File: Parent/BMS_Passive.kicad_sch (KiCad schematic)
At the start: 12 parts, among them U15 TSV911IDT, U16 TSV911IDT, U17 TSV911IDT, U18 TSV911IDT, U31 TSV911IDT, U32 TSV911IDT, U33 TSV911IDT, U34 TSV911IDT

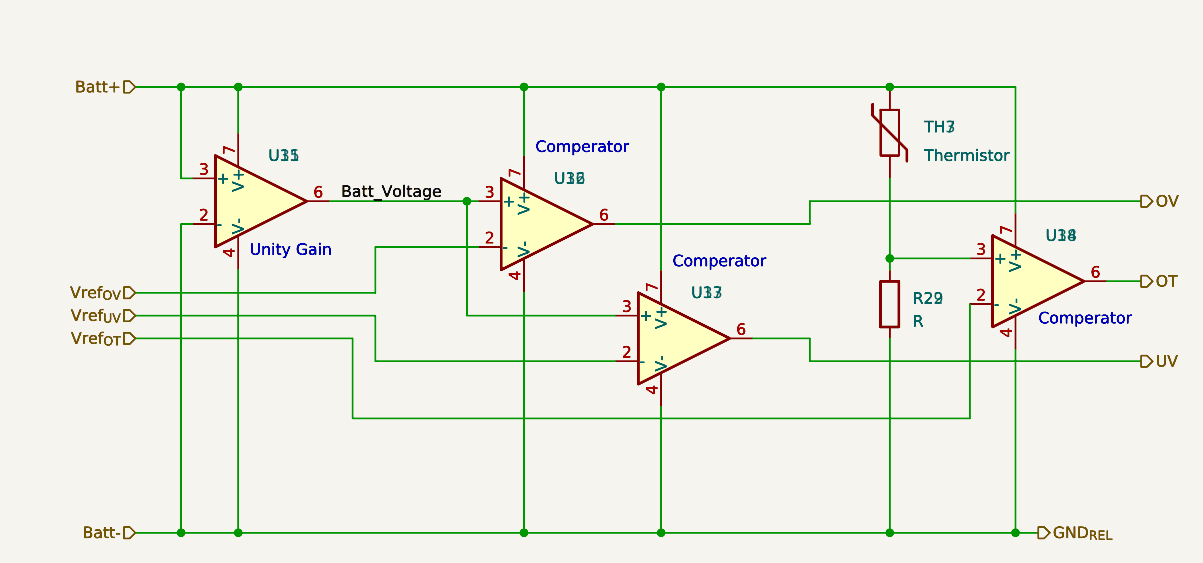
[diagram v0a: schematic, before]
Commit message: Updated Parent further - Move workspace to cloud
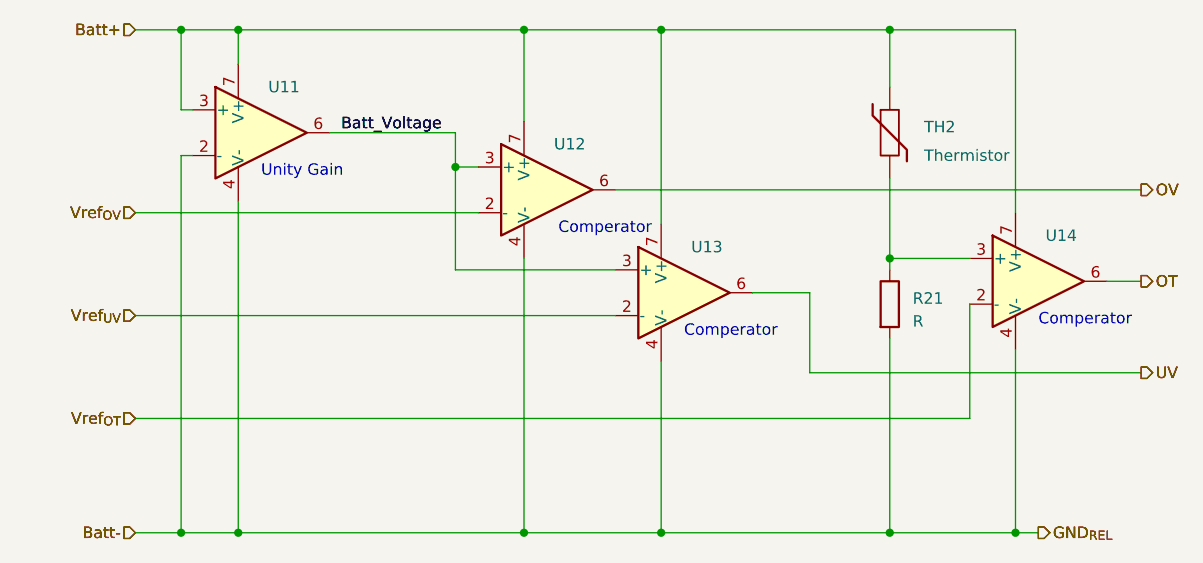
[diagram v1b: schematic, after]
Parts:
- removed R29: R, symbol Device:R
- removed TH7: Thermistor, symbol Device:Thermistor
- removed U15, U16, U33, U34: TSV911IDT, Package_SO:SOIC-8_3.9x4.9mm_P1.27mm, symbol Amplifier_Operational:TSV911IDT
- renumbered R22 to R21, TH3 to TH2, U31 to U11, U32 to U12, U17 to U13, U18 to U14
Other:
- moved on the sheet: U11, U12, U13

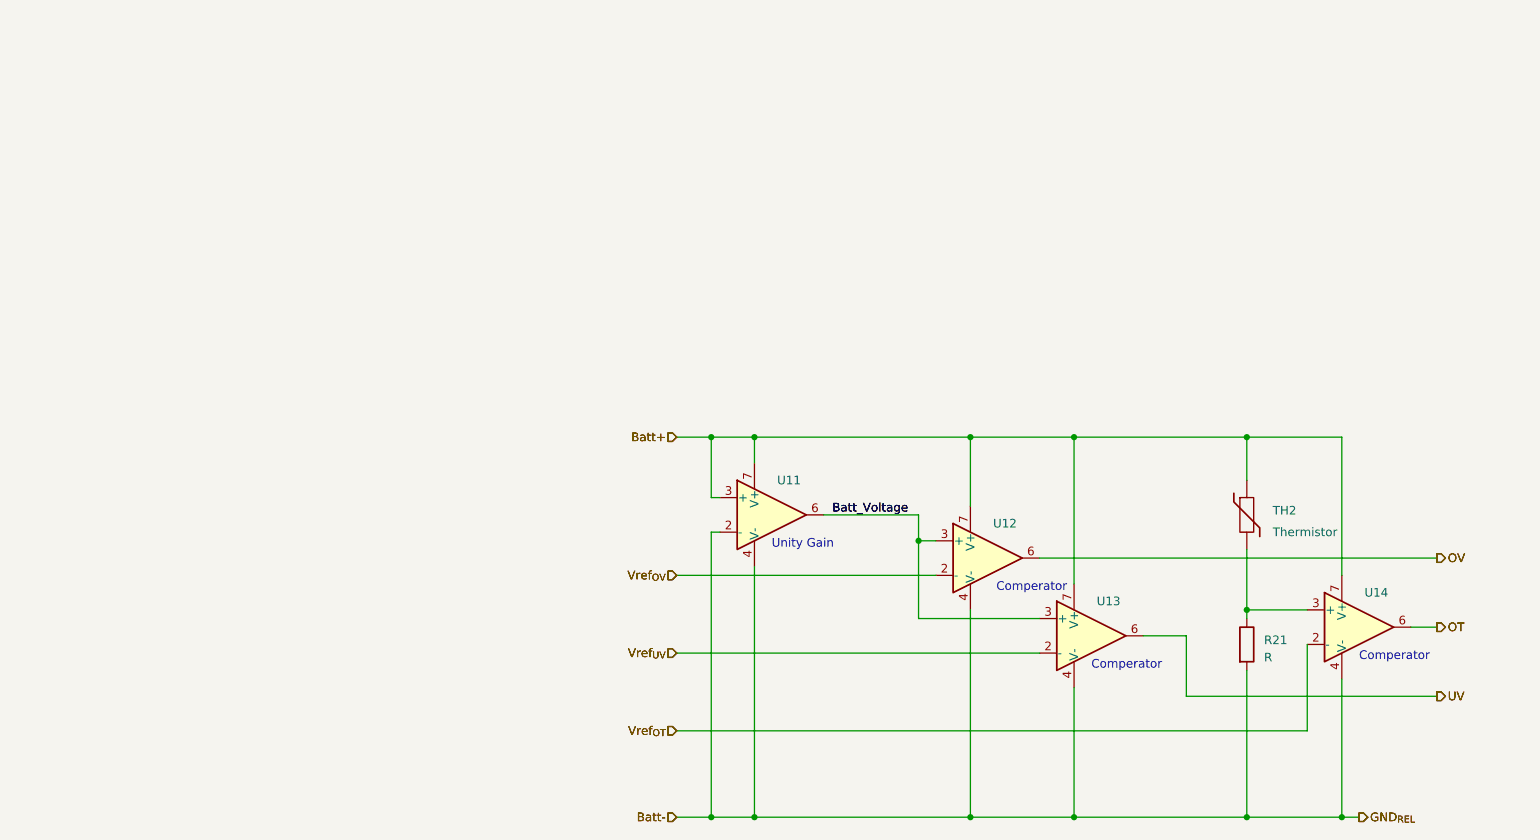
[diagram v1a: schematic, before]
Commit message: Updated Parent further - Move workspace to cloud
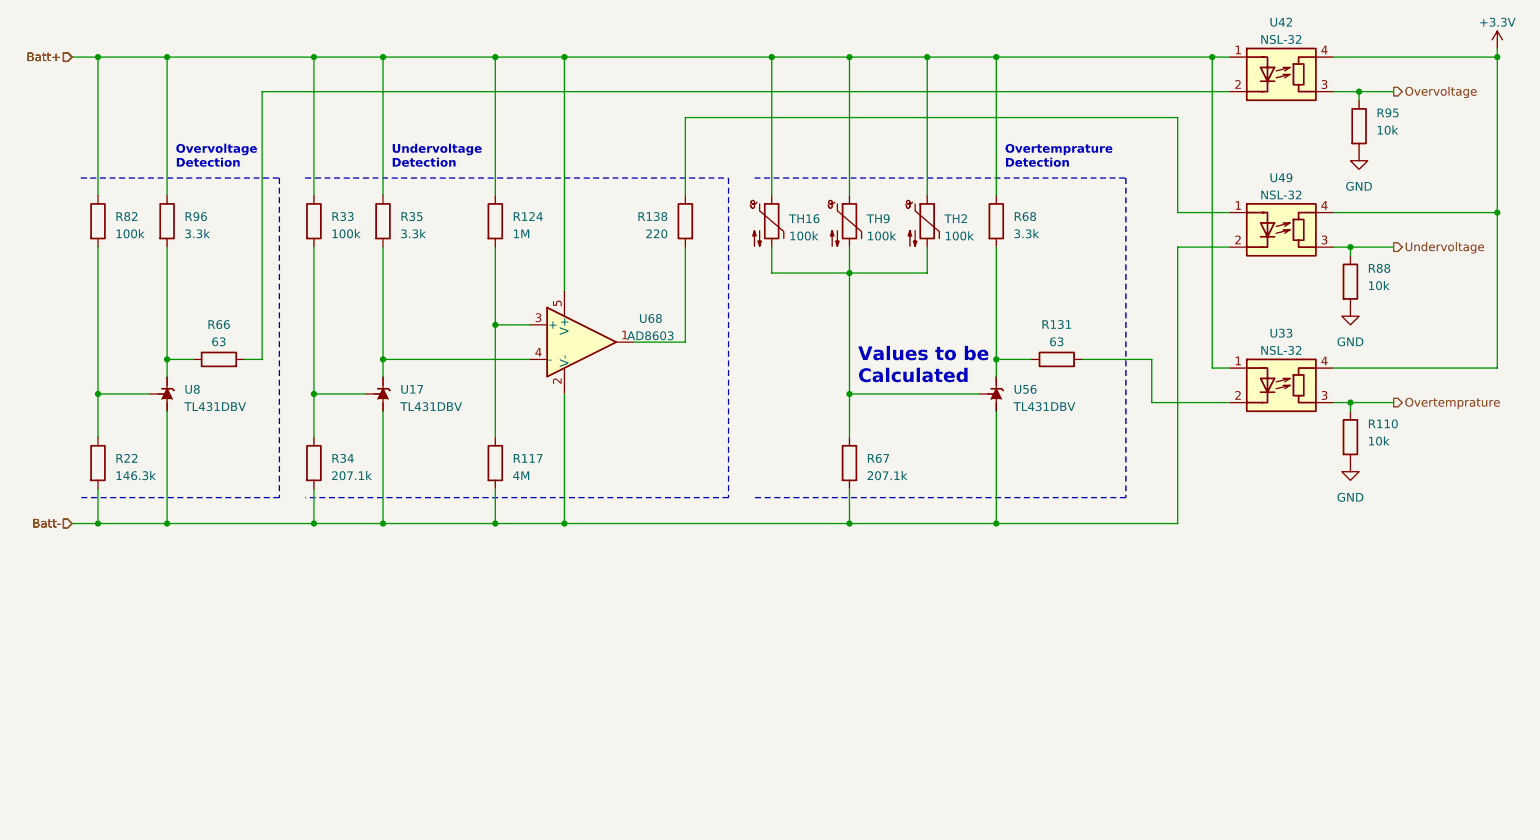
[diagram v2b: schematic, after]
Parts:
- removed R21: R, symbol Device:R
- removed TH2: Thermistor, symbol Device:Thermistor
- removed U11, U12, U13, U14: TSV911IDT, Package_SO:SOIC-8_3.9x4.9mm_P1.27mm, symbol Amplifier_Operational:TSV911IDT
- added R110, R88, R95: 10k, symbol Device:R
- added R117: 4M, symbol Device:R
- added R124: 1M, symbol Device:R
- added R131, R66: 63, symbol Device:R
- added R138: 220, symbol Device:R
- added R22: 146.3k, symbol Device:R
- added R33, R82: 100k, symbol Device:R
- added R34, R67: 207.1k, symbol Device:R
- added R35, R68, R96: 3.3k, symbol Device:R
- added TH16, TH2, TH9: 100k, symbol Device:Thermistor_NTC
- added U17, U56, U8: TL431DBV, Package_TO_SOT_SMD:SOT-23-5, symbol Reference_Voltage:TL431DBV
- added U33, U42, U49: NSL-32, OptoDevice:Luna_NSL-32, symbol Isolator:NSL-32
- added U68: AD8603, Package_TO_SOT_SMD:TSOT-23-5, symbol Amplifier_Operational:AD8603
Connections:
- net Batt+: now also R124.1, R33.1, R35.1, R68.1, R82.1, R96.1, TH16.1, TH2.1, TH9.1, U33.1 (A), U42.1 (A), U68.5 (V+)
- net Batt-: now also R117.2, R22.2, R34.2, R67.2, U17.5 (A), U49.2 (K), U56.5 (A), U68.2 (V-), U8.5 (A)
- new net: R138.2, U68.1
- new net: R117.1, R124.2, U68.3 (+)
- new net: R35.2, U17.3 (K), U68.4 (-)
- new net: R131.1, R68.2, U56.3 (K)
- new net: R67.1, TH16.2, TH2.2, TH9.2, U56.4 (REF)
- new net: R22.1, R82.2, U8.4 (REF)
- new net: R138.1, U49.1 (A)
- new net: R66.1, R96.2, U8.3 (K)
- new net: R66.2, U42.2 (K)
- new net: R33.2, R34.1, U17.4 (REF)
- new net: R131.2, U33.2 (K)
- new net +3.3V: U33.4 (R), U42.4 (R), U49.4 (R)
- new net GND: R110.2, R88.2, R95.2
- new net Overtemprature: R110.1, U33.3 (R)
- new net Overvoltage: R95.1, U42.3 (R)
- new net Undervoltage: R88.1, U49.3 (R)
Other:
- note added: "Overtemprature Detection"
- note added: "Overvoltage Detection"
- note added: "Undervoltage Detection"
- note added: "Values to be Calculated"
- note removed: "Comperator"
- note removed: "Unity Gain"

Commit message: Updated Parent - Moved workspace to cloud
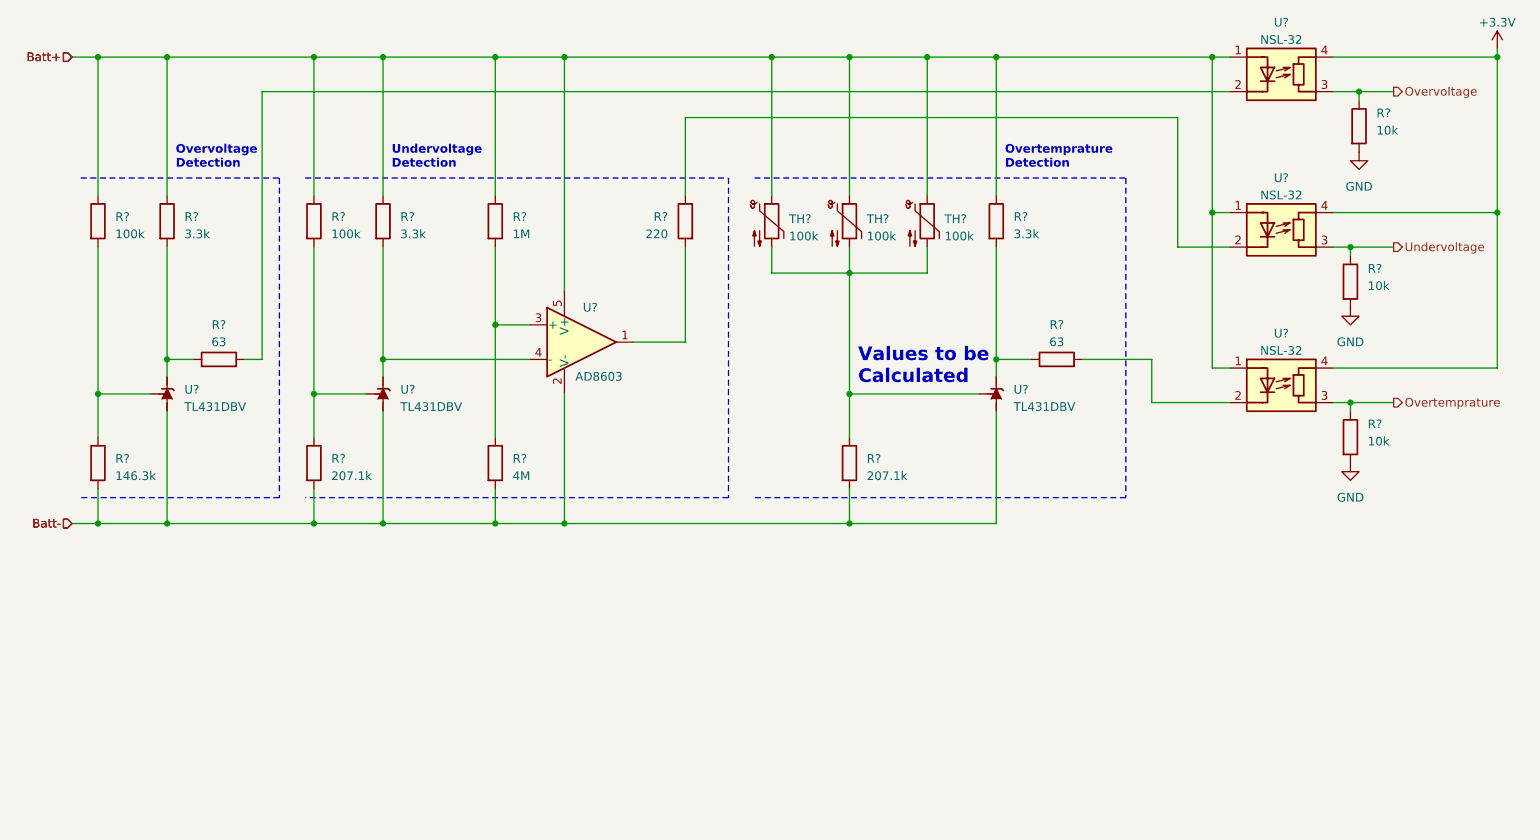
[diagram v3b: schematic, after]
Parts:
- renumbered R68 to R?, R67 to R?, R88 to R?, R82 to R?, R35 to R?, R66 to R?, R117 to R?, R96 to R?, R95 to R?, R110 to R?, R131 to R?, R34 to R?, R22 to R?, R33 to R?, R124 to R?, R138 to R?, TH2 to TH?, TH16 to TH?, TH9 to TH?, U68 to U?, U49 to U?, U56 to U?, U8 to U?, U17 to U?, U42 to U?, U33 to U?
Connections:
- net Batt+: now also U?.1 (A)
- net Batt-: no longer U?.2 (K)
- net at R?.1: now also U?.2 (K); no longer U?.1 (A)
